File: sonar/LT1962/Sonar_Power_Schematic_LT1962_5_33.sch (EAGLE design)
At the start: 34 parts, among them U1 LT3471', U2 LT1962-5, U3 LT1962-3.3, U4 LT1175

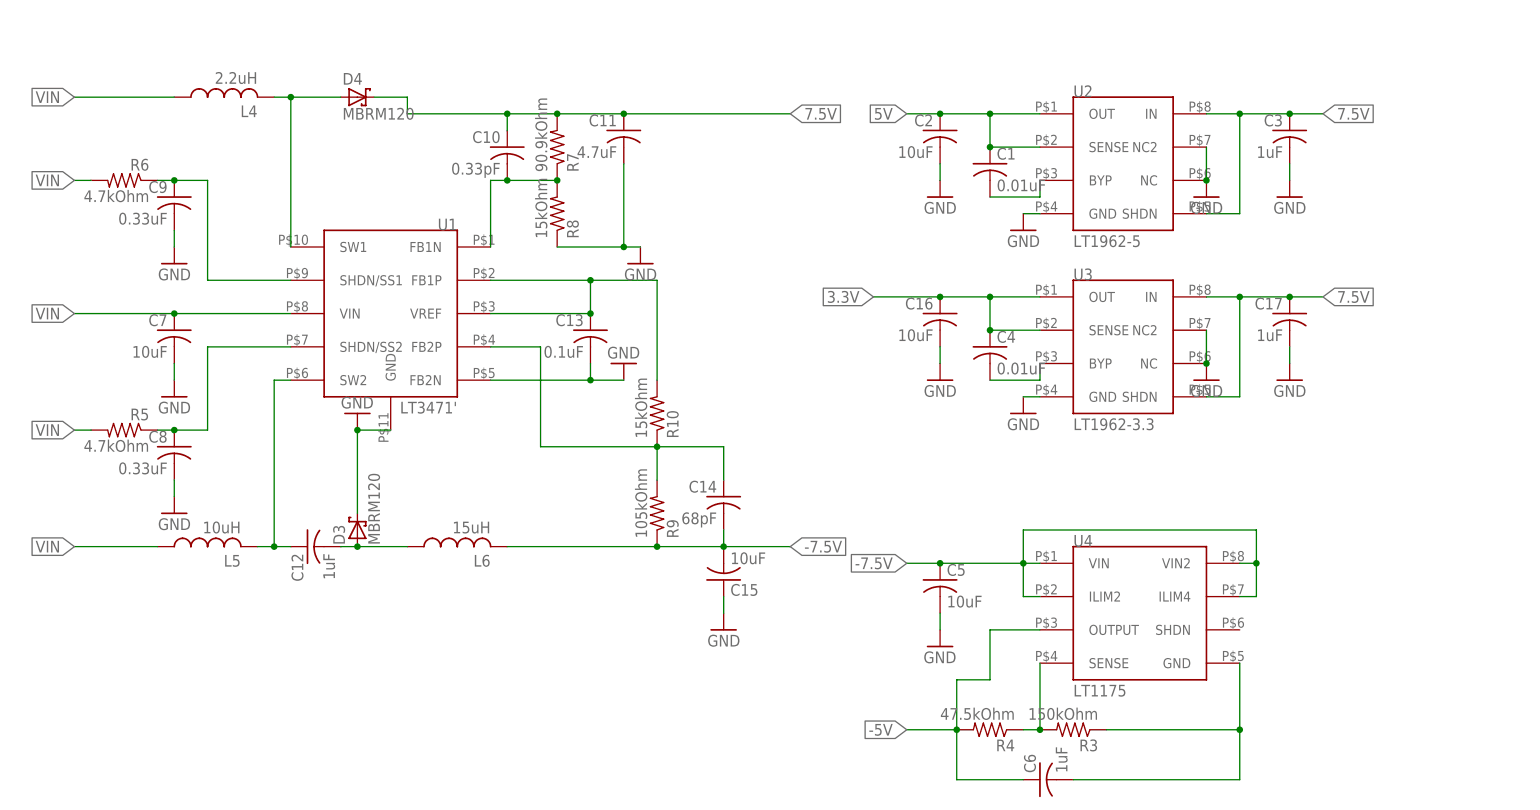
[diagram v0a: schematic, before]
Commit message: LT1117 and LT1962 schematics, PCBs, and design blocks
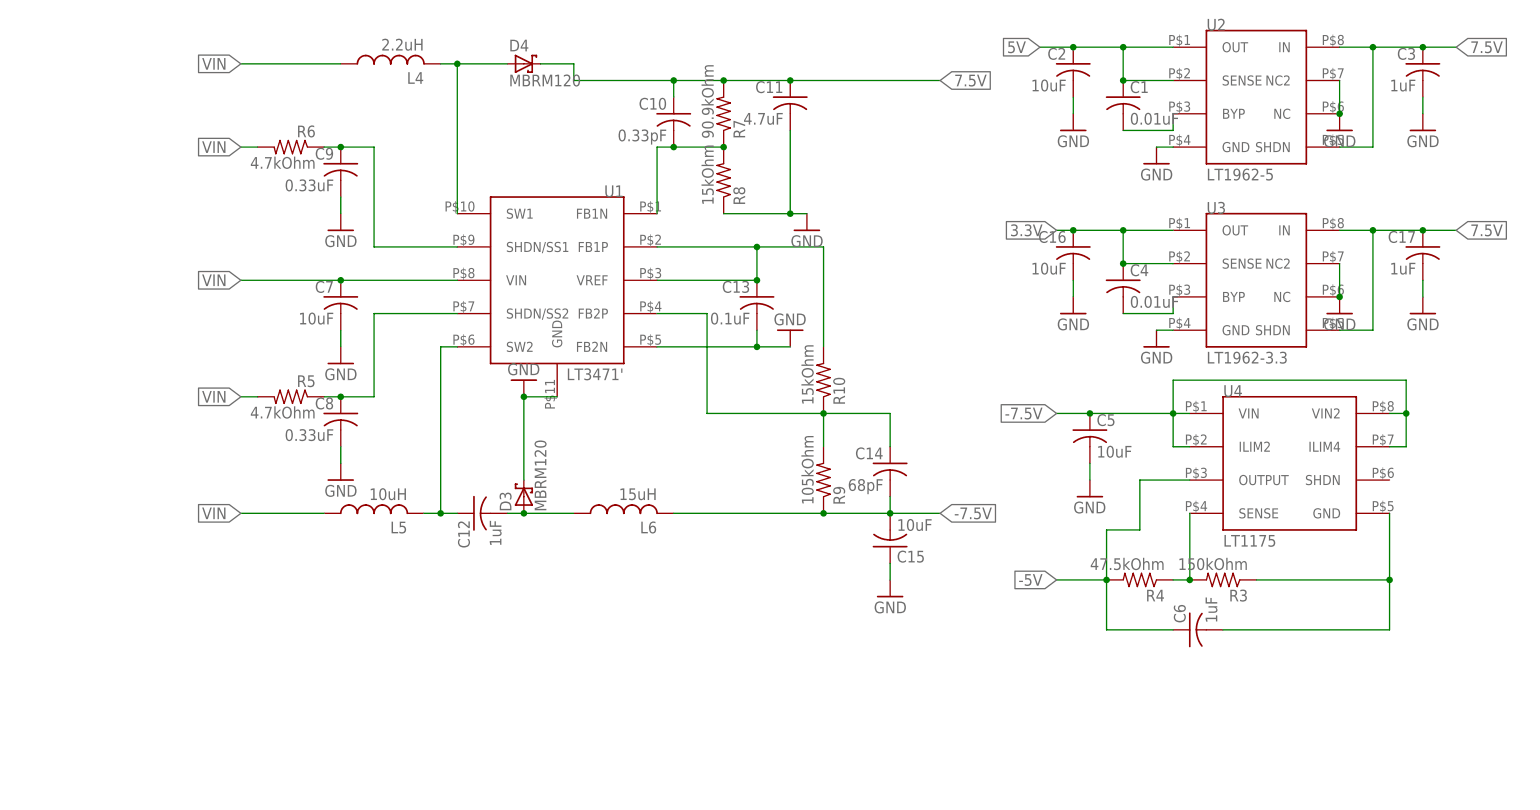
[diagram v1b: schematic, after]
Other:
- moved on the sheet: C1, C10, C11, C12, C13, C14, C15, C16, C17, C2, C3, C4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

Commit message: GND fixed
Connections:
- removed net N$10: C6.2, R3.1, U4.GND
- net GND: now also C6.2, R3.1, U4.GND
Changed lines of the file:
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@@
 <part name="GND15" library="supply1" library_urn="urn:adsk.eagle:library:371" deviceset="GND" device=""/>
 <part name="GND16" library="supply1" library_urn="urn:adsk.eagle:library:371" deviceset="GND" device=""/>
+<part name="GND17" library="supply1" library_urn="urn:adsk.eagle:library:371" deviceset="GND" device=""/>
 </parts>
 <sheets>
@@
 <instance part="GND15" gate="1" x="25.4" y="2.54" rot="MR0"/>
 <instance part="GND16" gate="1" x="78.74" y="2.54" rot="MR0"/>
+<instance part="GND17" gate="1" x="73.66" y="-48.26" rot="MR0"/>
 </instances>
 <busses>
@@
 <wire x1="78.74" y1="7.62" x2="78.74" y2="5.08" width="0.1524" layer="91"/>
 </segment>
+<segment>
+<pinref part="R3" gate="G$1" pin="1"/>
+<wire x1="53.34" y1="-38.1" x2="73.66" y2="-38.1" width="0.1524" layer="91"/>
+<pinref part="U4" gate="G$1" pin="GND"/>
+<wire x1="73.66" y1="-38.1" x2="73.66" y2="-27.94" width="0.1524" layer="91"/>
+<pinref part="C6" gate="G$1" pin="2"/>
+<wire x1="48.26" y1="-45.72" x2="73.66" y2="-45.72" width="0.1524" layer="91"/>
+<wire x1="73.66" y1="-45.72" x2="73.66" y2="-38.1" width="0.1524" layer="91"/>
+<junction x="73.66" y="-38.1"/>
+<pinref part="GND17" gate="1" pin="GND"/>
+<junction x="73.66" y="-45.72"/>
+</segment>
 </net>
 <net name="-5V" class="0">
@@
 </segment>
 </net>
-<net name="N$10" class="0">
-<segment>
-<pinref part="R3" gate="G$1" pin="1"/>
-<wire x1="53.34" y1="-38.1" x2="73.66" y2="-38.1" width="0.1524" layer="91"/>
-<pinref part="U4" gate="G$1" pin="GND"/>
-<wire x1="73.66" y1="-38.1" x2="73.66" y2="-27.94" width="0.1524" layer="91"/>
-<pinref part="C6" gate="G$1" pin="2"/>
-<wire x1="48.26" y1="-45.72" x2="73.66" y2="-45.72" width="0.1524" layer="91"/>
-<wire x1="73.66" y1="-45.72" x2="73.66" y2="-38.1" width="0.1524" layer="91"/>
-<junction x="73.66" y="-38.1"/>
-</segment>
-</net>
